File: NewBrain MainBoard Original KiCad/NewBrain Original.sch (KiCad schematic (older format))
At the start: 41 parts, among them U417 MC14584BDG, U418 74LS00, U425 74LS74, U426 74LS86, U429 74LS139, U431 74LS32, U432 74LS04, U433 74LS32, U434 74LS86, U435 74LS06, U437 74LS08, U438 74LS08, U439 74LS04, U440 74LS02, U441 74LS00, U443 74LS11, U444 74LS157_UNITS, U445 74LS112, U446 74LS21, U447 74LS393, U448 74LS10, U449 74LS157, U450 74LS04, U451 SN74LS279AN, U452 MC14584BDG_UNITS, U453 2716-Memory_EPROM, U455 74LS27, U456 74LS32, U457 74LS10, U459 74LS32, U460 74LS112, U462 74LS32, U463 74LS32, U464 74LS11, U465 74LS11, U466 74LS21, U467 74LS04, U468 74LS393, U469 74LS10, U470 74LS00, U471 74LS11

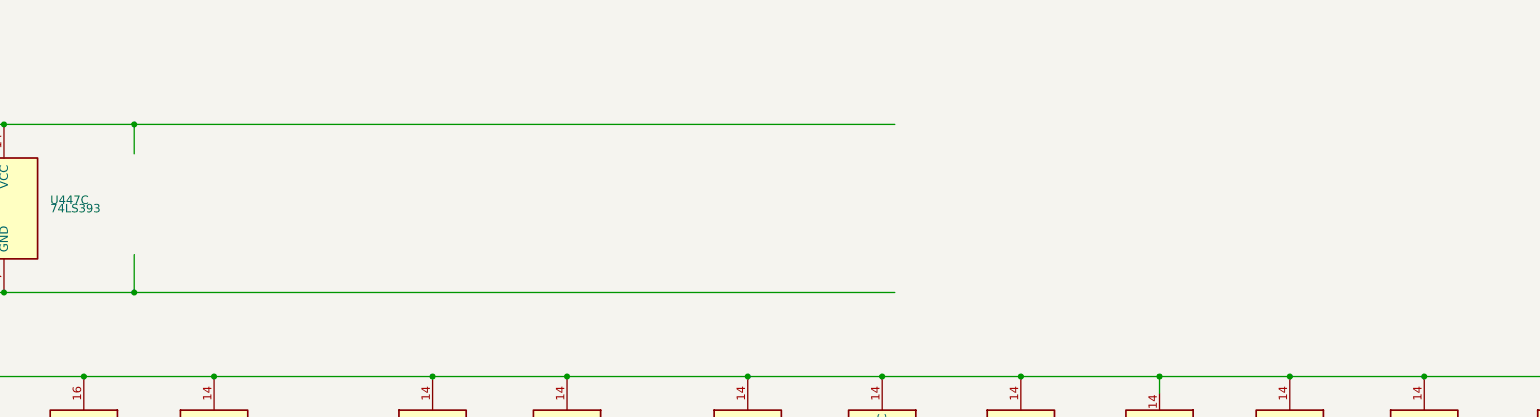
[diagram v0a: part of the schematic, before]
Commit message: UPdates add links and fix values add smoothing capacitors.
Signed-off-by: John Bradley <flypie@rocketmail.com>
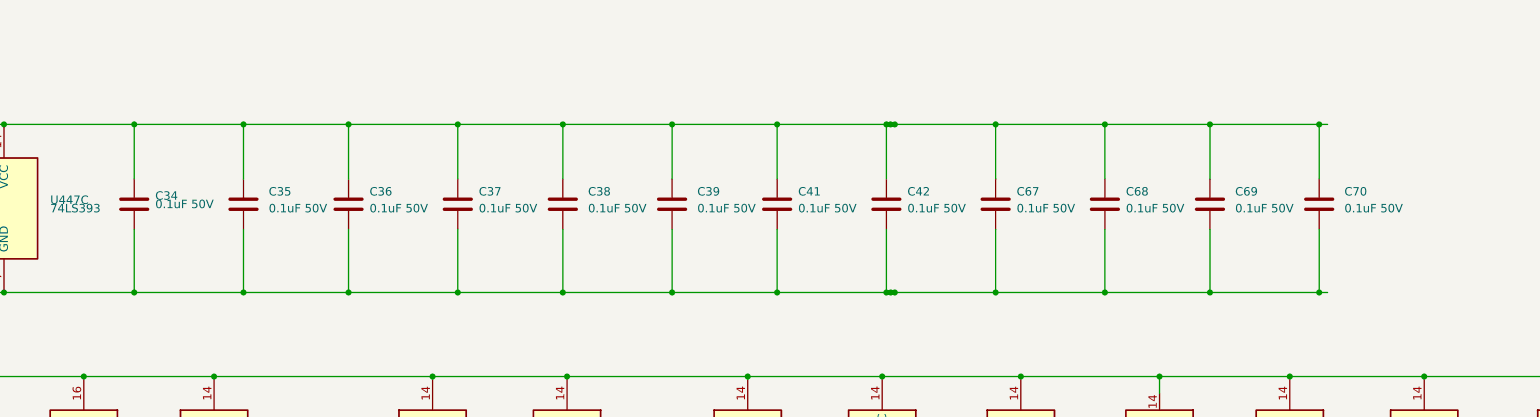
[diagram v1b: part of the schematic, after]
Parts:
- added C34, C35, C36, C37, C38, C39, C41, C42, C67, C68, C69, C70: 0.1uF 50V, Capacitor_THT:C_Axial_L3.8mm_D2.6mm_P7.50mm_Horizontal, symbol Device:C
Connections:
- wire segments 98 -> 142
